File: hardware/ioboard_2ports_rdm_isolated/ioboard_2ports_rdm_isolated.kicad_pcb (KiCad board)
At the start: 2 copper layers, 106 x 55 mm, 33 parts, among them J1 Conn_02x06_Odd_Even, J12 Conn_01x03, J2 XLR3, J3 XLR3, J4 8P8C, J5 8P8C, J6 Conn_01x03, J8 XLR3, J9 XLR3, U1 M24C64-RMN6TP, U2 CRE1S0505DC, U4 ADM2483xRW, U6 ADM2483xRW

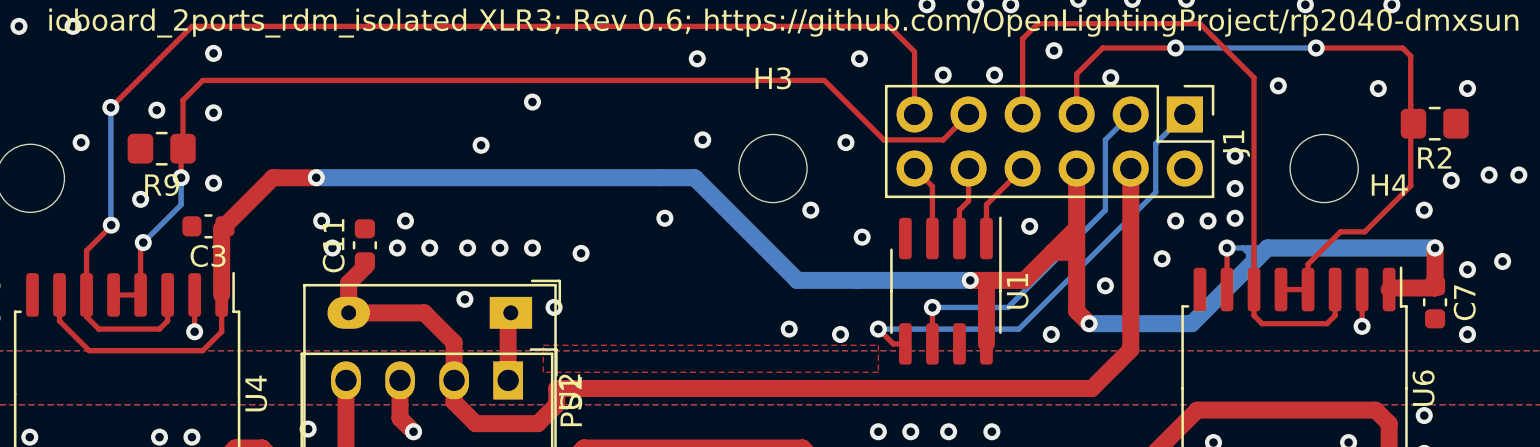
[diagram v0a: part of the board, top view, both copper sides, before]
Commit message: Update all footprints and ignore all other DRC warning on ioboards
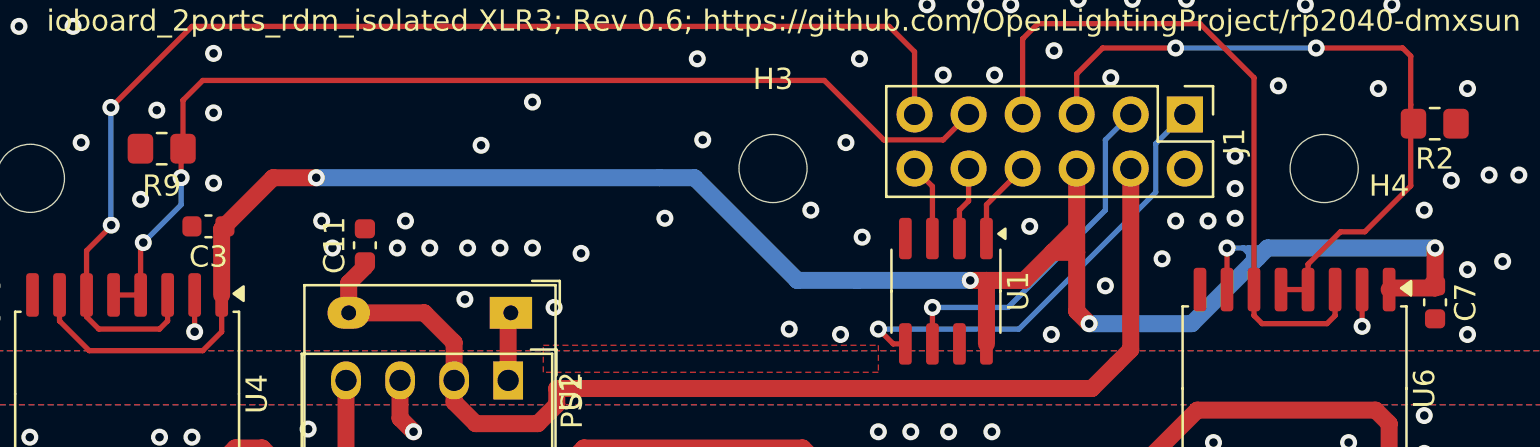
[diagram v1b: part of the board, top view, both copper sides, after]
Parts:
- PS1: footprint Converter_DCDC:Converter_DCDC_muRata_CRE1xxxxxx3C_THT -> Converter_DCDC:Converter_DCDC_Murata_CRE1xxxxxx3C_THT
- U2: footprint Converter_DCDC:Converter_DCDC_muRata_CRE1xxxxxxDC_THT -> Converter_DCDC:Converter_DCDC_Murata_CRE1xxxxxxDC_THT
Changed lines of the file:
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@@
 			(pintype "passive")
 		)
-		(model "${KISYS3DMOD}/Connector_PinHeader_2.54mm.3dshapes/PinHeader_2x06_P2.54mm_Vertical.wrl"
+		(model "${KICAD8_3DMODEL_DIR}/Connector_PinHeader_2.54mm.3dshapes/PinHeader_2x06_P2.54mm_Vertical.wrl"
 			(offset
 				(xyz 0 0 0)
@@
 			(pintype "passive")
 		)
-		(model "${KISYS3DMOD}/Resistor_SMD.3dshapes/R_0603_1608Metric.wrl"
+		(model "${KICAD8_3DMODEL_DIR}/Resistor_SMD.3dshapes/R_0603_1608Metric.wrl"
 			(offset
 				(xyz 0 0 0)
@@
 		)
 		(fp_line
-			(start -3.86 -5.005)
-			(end -5.675 -5.005)
-			(stroke
-				(width 0.12)
-				(type solid)
-			)
-			(layer "F.SilkS")
-		)
-		(fp_line
 			(start -3.86 -5.26)
 			(end -3.86 -5.005)
@@
 			(layer "F.SilkS")
 		)
+		(fp_poly
+			(pts
+				(xy -4.7125 -5.005) (xy -5.0525 -5.475) (xy -4.3725 -5.475) (xy -4.7125 -5.005)
+			)
+			(stroke
+				(width 0.12)
+				(type solid)
+			)
+			(fill solid)
+			(layer "F.SilkS")
+		)
 		(fp_line
 			(start -5.93 5.4)
@@
 			(pintype "power_in")
 		)
-		(model "${KISYS3DMOD}/Package_SO.3dshapes/SOIC-16W_7.5x10.3mm_P1.27mm.wrl"
+		(model "${KICAD8_3DMODEL_DIR}/Package_SO.3dshapes/SOIC-16W_7.5x10.3mm_P1.27mm.wrl"
 			(offset
 				(xyz 0 0 0)
@@
 			(pintype "passive")
 		)
-		(model "${KISYS3DMOD}/Capacitor_SMD.3dshapes/C_0603_1608Metric.wrl"
+		(model "${KICAD8_3DMODEL_DIR}/Capacitor_SMD.3dshapes/C_0603_1608Metric.wrl"
 			(offset
 				(xyz 0 0 0)
@@
 			(pintype "passive")
 		)
-		(model "${KISYS3DMOD}/Resistor_SMD.3dshapes/R_0603_1608Metric.wrl"
+		(model "${KICAD8_3DMODEL_DIR}/Resistor_SMD.3dshapes/R_0603_1608Metric.wrl"
 			(offset
 				(xyz 0 0 0)
@@
 			(pintype "passive")
 		)
-		(model "${KISYS3DMOD}/Resistor_SMD.3dshapes/R_0603_1608Metric.wrl"
+		(model "${KICAD8_3DMODEL_DIR}/Resistor_SMD.3dshapes/R_0603_1608Metric.wrl"
 			(offset
 				(xyz 0 0 0)
@@
 			(size 1.2 1.4)
 			(layers "F.Cu" "F.Paste" "F.Mask")
-			(roundrect_rratio 0.2083325)
+			(roundrect_rratio 0.208333)
 			(net 9 "GND")
 			(pintype "passive")
@@
 			(size 1.2 1.4)
 			(layers "F.Cu" "F.Paste" "F.Mask")
-			(roundrect_rratio 0.2083325)
+			(roundrect_rratio 0.208333)
 			(net 4 "/GP1")
 			(pintype "passive")
 		)
-		(model "${KISYS3DMOD}/Resistor_SMD.3dshapes/R_0805_2012Metric.wrl"
+		(model "${KICAD8_3DMODEL_DIR}/Resistor_SMD.3dshapes/R_0805_2012Metric.wrl"
 			(offset
 				(xyz 0 0 0)
@@
 			(pintype "passive")
 		)
-		(model "${KISYS3DMOD}/Capacitor_SMD.3dshapes/C_0603_1608Metric.wrl"
+		(model "${KICAD8_3DMODEL_DIR}/Capacitor_SMD.3dshapes/C_0603_1608Metric.wrl"
 			(offset
 				(xyz 0 0 0)
@@
 		)
 	)
-	(footprint "Converter_DCDC:Converter_DCDC_muRata_CRE1xxxxxxDC_THT"
+	(footprint "Converter_DCDC:Converter_DCDC_Murata_CRE1xxxxxxDC_THT"
 		(layer "F.Cu")
 		(at 52.578 36.322 -90)
@@
 		(tags "Isloated DC-DC")
 		(property "Reference" "U2"
-			(at 3.7 -2.8 90)
+			(at 3.7 -2.8 -90)
 			(layer "F.SilkS")
 			(effects
@@
 		)
 		(property "Value" "CRE1S0505DC"
-			(at 3.3 10.7 90)
+			(at 3.3 10.7 -90)
 			(layer "F.Fab")
 			(effects
@@
 			)
 		)
-		(property "Footprint" "Converter_DCDC:Converter_DCDC_muRata_CRE1xxxxxxDC_THT"
+		(property "Footprint" "Converter_DCDC:Converter_DCDC_Murata_CRE1xxxxxxDC_THT"
 			(at 0 0 -90)
+			(unlocked yes)
 			(layer "F.Fab")
 			(hide yes)
@@
 		(property "Datasheet" "http://power.murata.com/datasheet?/data/power/ncl/kdc_cre1.pdf"
 			(at 0 0 -90)
+			(unlocked yes)
 			(layer "F.Fab")
 			(hide yes)
@@
 		(property "Description" ""
 			(at 0 0 -90)
+			(unlocked yes)
 			(layer "F.Fab")
 			(hide yes)
@@
 		)
 		(fp_text user "${REFERENCE}"
-			(at 3.81 3.81 90)
+			(at 3.81 3.81 -90)
 			(layer "F.Fab")
 			(effects
@@
 			(pintype "power_out")
 		)
-		(model "${KISYS3DMOD}/Converter_DCDC.3dshapes/Converter_DCDC_muRata_CRE1xxxxxxDC_THT.wrl"
+		(model "${KICAD8_3DMODEL_DIR}/Converter_DCDC.3dshapes/Converter_DCDC_Murata_CRE1xxxxxxDC_THT.wrl"
 			(offset
 				(xyz 0 0 0)
@@
 		(fp_line
 			(start 0 -2.56)
-			(end -3.45 -2.56)
+			(end -1.95 -2.56)
 			(stroke
 				(width 0.12)
@@
 			(layer "F.SilkS")
 		)
+		(fp_poly
+			(pts
+				(xy -2.7 -2.465) (xy -2.94 -2.795) (xy -2.46 -2.795) (xy -2.7 -2.465)
+			)
+			(stroke
+				(width 0.12)
+				(type solid)
+			)
+			(fill solid)
+			(layer "F.SilkS")
+		)
 		(fp_line
 			(start -3.7 2.7)
@@
 			(pintype "power_in")
 		)
-		(model "${KISYS3DMOD}/Package_SO.3dshapes/SOIC-8_3.9x4.9mm_P1.27mm.wrl"
+		(model "${KICAD8_3DMODEL_DIR}/Package_SO.3dshapes/SOIC-8_3.9x4.9mm_P1.27mm.wrl"
 			(offset
 				(xyz 0 0 0)
@@
 			(pintype "passive")
 		)
-		(model "${KISYS3DMOD}/Capacitor_SMD.3dshapes/C_0603_1608Metric.wrl"
+		(model "${KICAD8_3DMODEL_DIR}/Capacitor_SMD.3dshapes/C_0603_1608Metric.wrl"
 			(offset
 				(xyz 0 0 0)
@@
 			(pintype "passive")
 		)
-		(model "${KISYS3DMOD}/Connector_PinHeader_2.54mm.3dshapes/PinHeader_1x03_P2.54mm_Vertical.wrl"
+		(model "${KICAD8_3DMODEL_DIR}/Connector_PinHeader_2.54mm.3dshapes/PinHeader_1x03_P2.54mm_Vertical.wrl"
 			(offset
 				(xyz 0 0 0)
@@
 			(pintype "passive")
 		)
-		(model "${KICAD6_3DMODEL_DIR}/Connector_Audio.3dshapes/Jack_XLR_Neutrik_NC3FAAH_Horizontal.wrl"
+		(model "${KICAD8_3DMODEL_DIR}/Connector_Audio.3dshapes/Jack_XLR_Neutrik_NC3FAAH_Horizontal.wrl"
 			(offset
 				(xyz 0 0 0)
@@
 			(pintype "passive")
 		)
-		(model "${KISYS3DMOD}/Capacitor_SMD.3dshapes/C_0603_1608Metric.wrl"
+		(model "${KICAD8_3DMODEL_DIR}/Capacitor_SMD.3dshapes/C_0603_1608Metric.wrl"
 			(offset
 				(xyz 0 0 0)
@@
 			(pintype "passive")
 		)
-		(model "${KICAD6_3DMODEL_DIR}/Connector_Audio.3dshapes/Jack_XLR_Neutrik_NC3FAAH_Horizontal.wrl"
+		(model "${KICAD8_3DMODEL_DIR}/Connector_Audio.3dshapes/Jack_XLR_Neutrik_NC3FAAH_Horizontal.wrl"
 			(offset
 				(xyz 0 0 0)
@@
 			(pintype "passive")
 		)
-		(model "${KISYS3DMOD}/Connector_PinHeader_2.54mm.3dshapes/PinHeader_1x03_P2.54mm_Vertical.wrl"
+		(model "${KICAD8_3DMODEL_DIR}/Connector_PinHeader_2.54mm.3dshapes/PinHeader_1x03_P2.54mm_Vertical.wrl"
 			(offset
 				(xyz 0 0 0)
@@
 			(pintype "passive")
 		)
-		(model "${KISYS3DMOD}/Resistor_SMD.3dshapes/R_0603_1608Metric.wrl"
+		(model "${KICAD8_3DMODEL_DIR}/Resistor_SMD.3dshapes/R_0603_1608Metric.wrl"
 			(offset
 				(xyz 0 0 0)
@@
 			(pintype "passive")
 		)
-		(model "${KISYS3DMOD}/Resistor_SMD.3dshapes/R_0603_1608Metric.wrl"
+		(model "${KICAD8_3DMODEL_DIR}/Resistor_SMD.3dshapes/R_0603_1608Metric.wrl"
 			(offset
 				(xyz 0 0 0)
@@
 		)
 		(fp_line
-			(start -3.86 -5.005)
-			(end -5.675 -5.005)
-			(stroke
-				(width 0.12)
-				(type solid)
-			)
-			(layer "F.SilkS")
-		)
-		(fp_line
 			(start -3.86 -5.26)
 			(end -3.86 -5.005)
@@
 			(layer "F.SilkS")
 		)
+		(fp_poly
+			(pts
+				(xy -4.7125 -5.005) (xy -5.0525 -5.475) (xy -4.3725 -5.475) (xy -4.7125 -5.005)
+			)
+			(stroke
+				(width 0.12)
+				(type solid)
+			)
+			(fill solid)
+			(layer "F.SilkS")
+		)
 		(fp_line
 			(start -5.93 5.4)
@@
 			(pintype "power_in")
 		)
-		(model "${KISYS3DMOD}/Package_SO.3dshapes/SOIC-16W_7.5x10.3mm_P1.27mm.wrl"
+		(model "${KICAD8_3DMODEL_DIR}/Package_SO.3dshapes/SOIC-16W_7.5x10.3mm_P1.27mm.wrl"
 			(offset
 				(xyz 0 0 0)
@@
 			(pintype "passive")
 		)
-		(model "${KISYS3DMOD}/Capacitor_SMD.3dshapes/C_0603_1608Metric.wrl"
+		(model "${KICAD8_3DMODEL_DIR}/Capacitor_SMD.3dshapes/C_0603_1608Metric.wrl"
 			(offset
 				(xyz 0 0 0)
@@
 			(pintype "passive")
 		)
-		(model "${KISYS3DMOD}/Resistor_SMD.3dshapes/R_0603_1608Metric.wrl"
+		(model "${KICAD8_3DMODEL_DIR}/Resistor_SMD.3dshapes/R_0603_1608Metric.wrl"
 			(offset
 				(xyz 0 0 0)
@@
 			(pintype "passive")
 		)
-		(model "${KISYS3DMOD}/Capacitor_SMD.3dshapes/C_0603_1608Metric.wrl"
+		(model "${KICAD8_3DMODEL_DIR}/Capacitor_SMD.3dshapes/C_0603_1608Metric.wrl"
 			(offset
 				(xyz 0 0 0)
@@
 		)
 	)
-	(footprint "Converter_DCDC:Converter_DCDC_muRata_CRE1xxxxxx3C_THT"
+	(footprint "Converter_DCDC:Converter_DCDC_Murata_CRE1xxxxxx3C_THT"
 		(layer "F.Cu")
 		(at 52.451 39.497 -90)
@@
 		(tags "Isolated 1W single output DC/DC")
 		(property "Reference" "PS1"
-			(at 1 -3 90)
+			(at 1 -3 -90)
 			(layer "F.SilkS")
 			(effects
@@
 		)
 		(property "Value" "MEE1S0503SC"
-			(at 2 11 -90)
+			(at 2 11 90)
 			(layer "F.Fab")
 			(effects
@@
 			)
 		)
-		(property "Footprint" "Converter_DCDC:Converter_DCDC_muRata_CRE1xxxxxx3C_THT"
+		(property "Footprint" "Converter_DCDC:Converter_DCDC_Murata_CRE1xxxxxx3C_THT"
 			(at 0 0 -90)
+			(unlocked yes)
 			(layer "F.Fab")
 			(hide yes)
@@
 		(property "Datasheet" "https://power.murata.com/pub/data/power/ncl/kdc_mee1.pdf"
 			(at 0 0 -90)
+			(unlocked yes)
 			(layer "F.Fab")
 			(hide yes)
@@
 		(property "Description" ""
 			(at 0 0 -90)
+			(unlocked yes)
 			(layer "F.Fab")
 			(hide yes)
@@
 			(pintype "power_out")
 		)
-		(model "${KISYS3DMOD}/Converter_DCDC.3dshapes/Converter_DCDC_muRata_CRE1xxxxxx3C_THT.wrl"
+		(model "${KICAD8_3DMODEL_DIR}/Converter_DCDC.3dshapes/Converter_DCDC_Murata_CRE1xxxxxx3C_THT.wrl"
 			(offset
 				(xyz 0 0 0)
@@
 			(pintype "passive")
 		)
-		(model "${KISYS3DMOD}/Resistor_SMD.3dshapes/R_0805_2012Metric.wrl"
+		(model "${KICAD8_3DMODEL_DIR}/Resistor_SMD.3dshapes/R_0805_2012Metric.wrl"
 			(offset
 				(xyz 0 0 0)
